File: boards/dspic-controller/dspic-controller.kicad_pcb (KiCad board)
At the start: 2 copper layers, 100 x 60 mm, 79 parts, among them J1 Power Input, J10 LowSide0, J11 LowSide1, J12 Speaker, J13 HighSide0, J14 HighSide1, J15 LED Matrix, J16 Enable0, J17 Enable1, J18 HF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

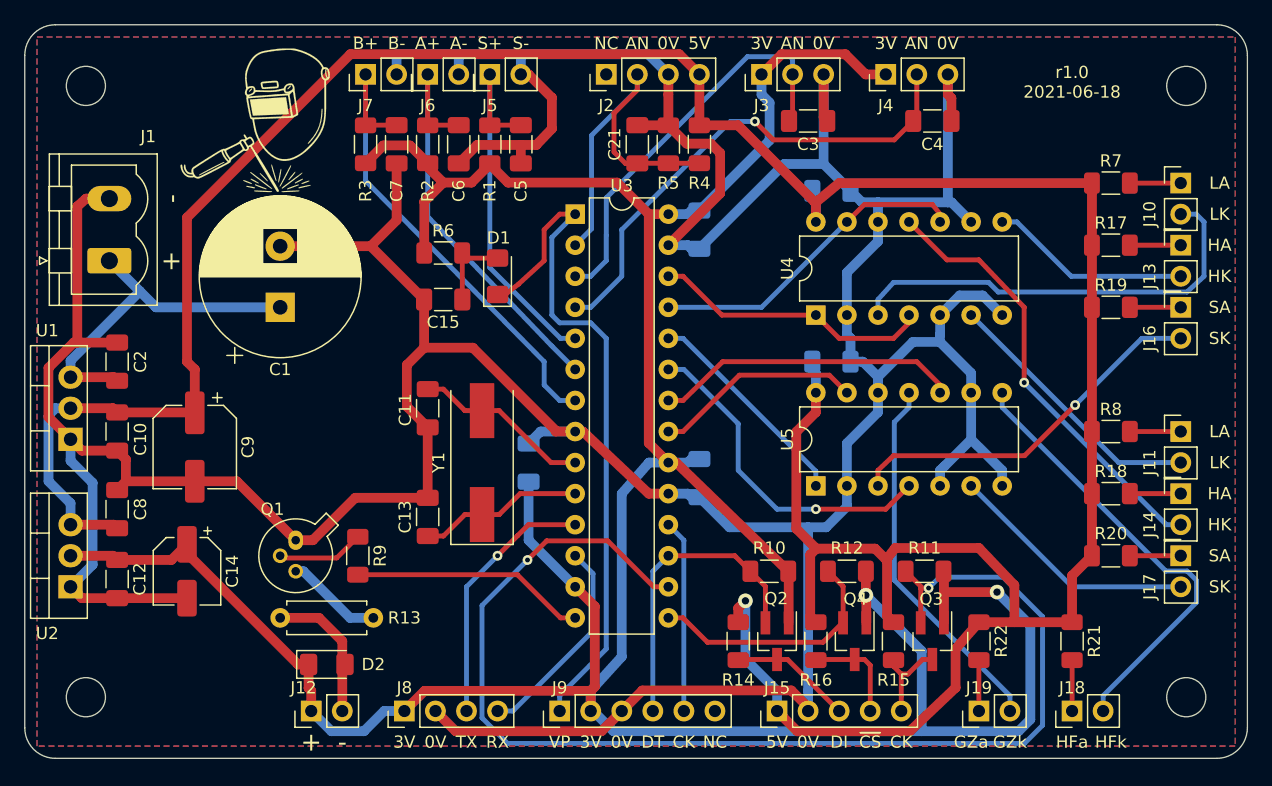
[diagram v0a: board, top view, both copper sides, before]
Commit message: dspic-controller: updated the project to kicad 7
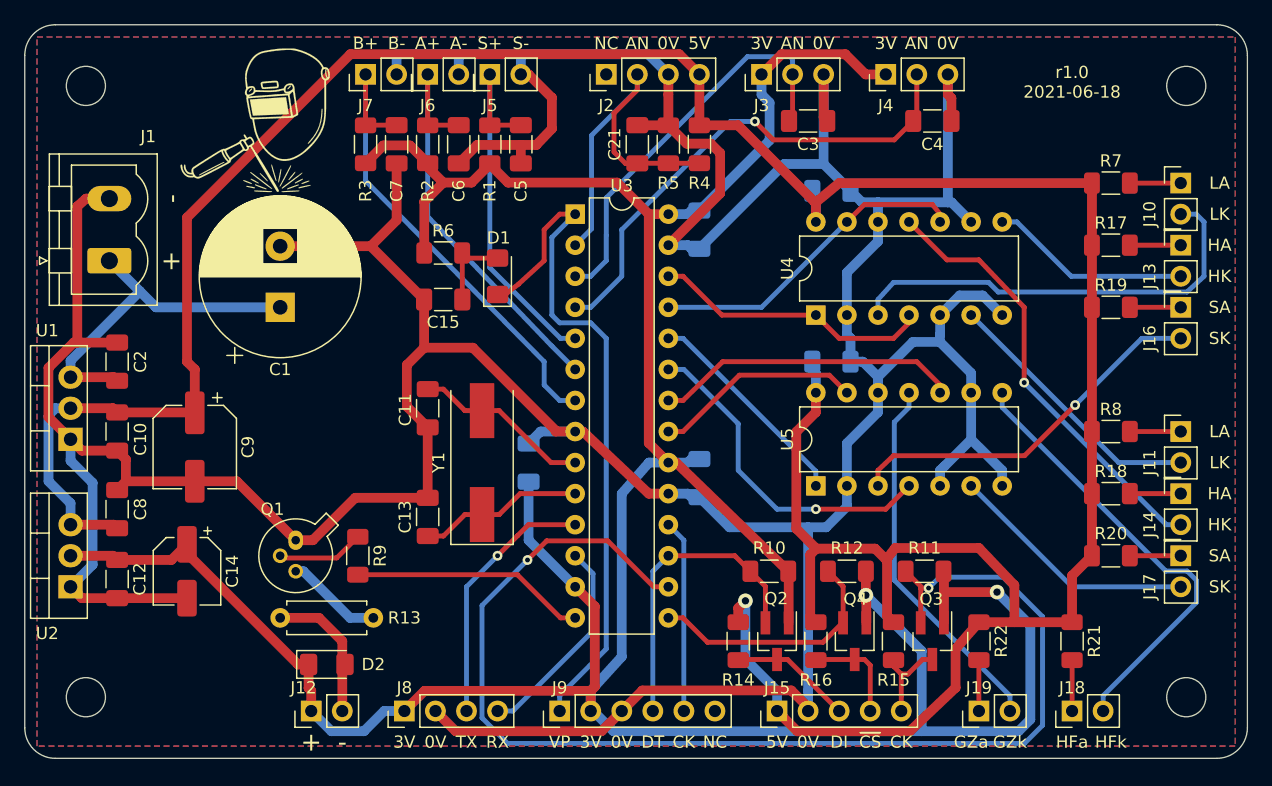
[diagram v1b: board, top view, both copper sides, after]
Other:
- net class Default removed
- net class Power removed
- board text added: "~{CS}"
- board text removed: "~CS"
